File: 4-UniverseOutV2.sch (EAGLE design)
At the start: 45 parts, among them IC1 MAX481, IC2 MAX481, IC3 MAX481, IC4 MAX481, U1 MC3FAH1, U2 MC3FAH1, U3 MC3FAH1, U4 MC3FAH1

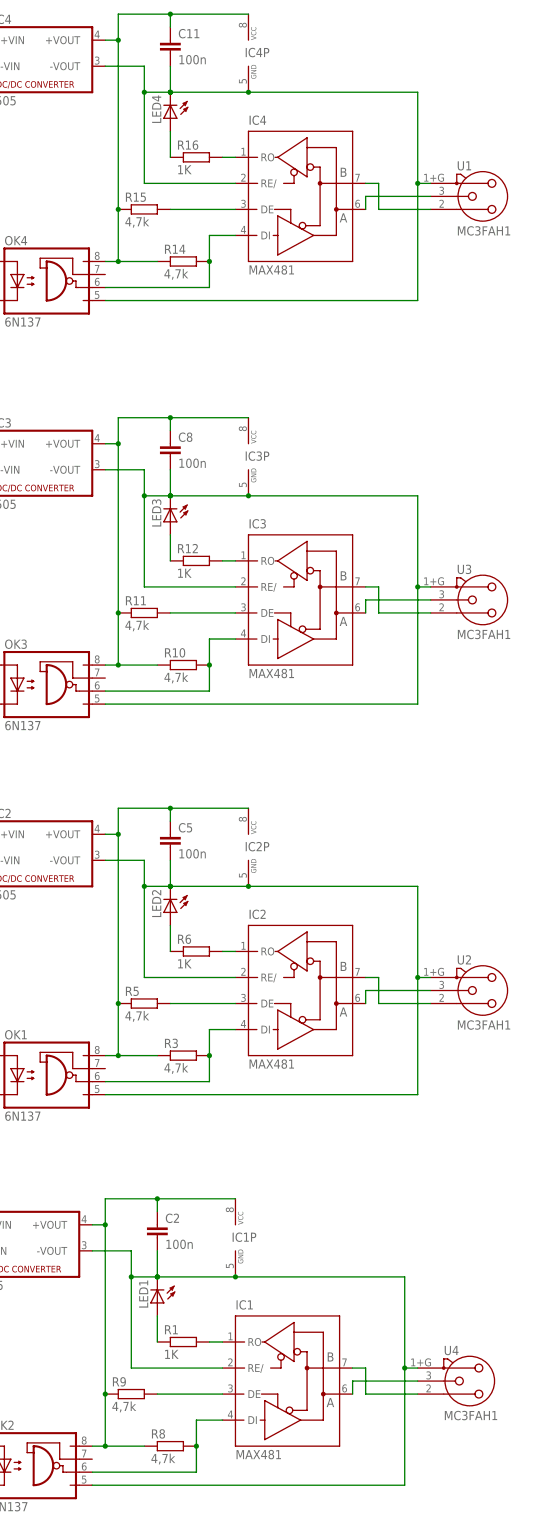
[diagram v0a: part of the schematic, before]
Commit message: Add files via upload
Added 120ohm resistors
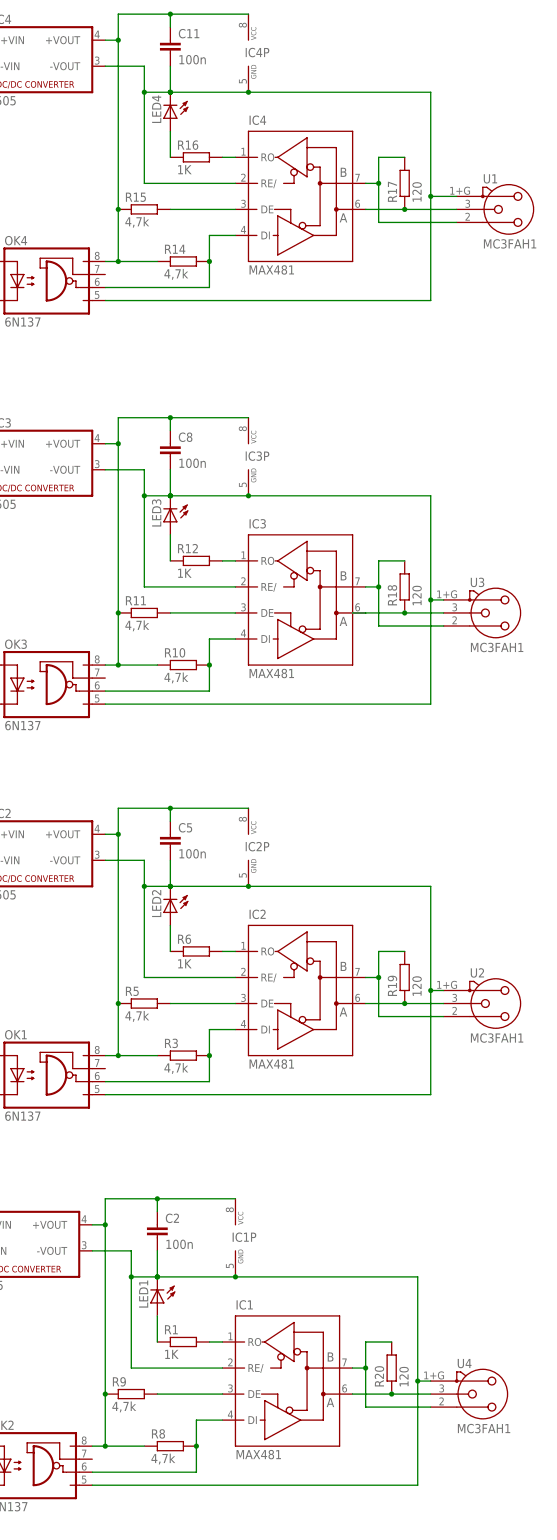
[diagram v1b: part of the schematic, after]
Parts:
- added R17, R18, R19, R20: 120, resistor:R-EU_0207/2V
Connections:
- net N$161: now also R20.1
- net N$162: now also R20.2
- net N$169: now also R19.1
- net N$170: now also R19.2
- net N$179: now also R18.1
- net N$181: now also R18.2
- net N$193: now also R17.1
- net N$194: now also R17.2
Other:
- moved on the sheet: U1, U2, U3, U4
